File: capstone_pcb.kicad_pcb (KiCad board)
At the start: 4 copper layers, 60.2 x 43.6 mm, 43 parts, among them IC6 BSS138, Q1 BSS138, U2 BMI270, U3 NRF52840-QIAA-R, U4 MAX30102, U5 AMS1117-1.8, U6 TPS61099DRV, X1 32MHz, X2 32.768kHz

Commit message: update pcb layout
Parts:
- moved C23 28.8 mm to (116.2, 64.7), turned to -90 degrees
- moved R7 26.2 mm to (116.2, 67.7), turned to 90 degrees
- moved C24 23.8 mm to (100.3, 50.3), turned to -90 degrees
- moved U4 21.0 mm to (112.2, 65.7), turned to 0 degrees
- moved R8 19.5 mm to (108.3, 50.2), turned to -90 degrees
- moved R9 19.5 mm to (108.3, 48.4)
- moved U5 19.4 mm to (114.8, 53.6), turned to -90 degrees
- moved U6 19.0 mm to (104.3, 50.3)
- moved R6 16.8 mm to (107.4, 64.5), turned to 90 degrees
- moved R4 11.4 mm to (107.4, 67.7), turned to -90 degrees
- moved BT1 9.00 mm to (93.3, 65.7), turned to -90 degrees
- moved X1 3.59 mm to (128.4, 71.1), turned to 90 degrees
- moved C1 2.16 mm to (130.9, 72.1), turned to 180 degrees
- moved C2 0.55 mm to (125.9, 72.1), turned to 0 degrees
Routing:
- net +1V8: track 83.7 -> 51.0 mm, vias 4 -> 3
- net /BSDA: track 9.35 -> 27.4 mm, vias 1 -> 2
- net /BSCL: track 9.48 -> 13.9 mm
- net +3V3: track 59.9 -> 62.5 mm, vias 12 -> 11
- net Net-(U3-XC2): track 7.67 -> 5.27 mm
- net +3V: track 10.9 -> 12.7 mm
- net Net-(U3-XC1): track 8.40 -> 7.28 mm
- net GND: track 61.3 -> 61.2 mm, vias 18 -> 21

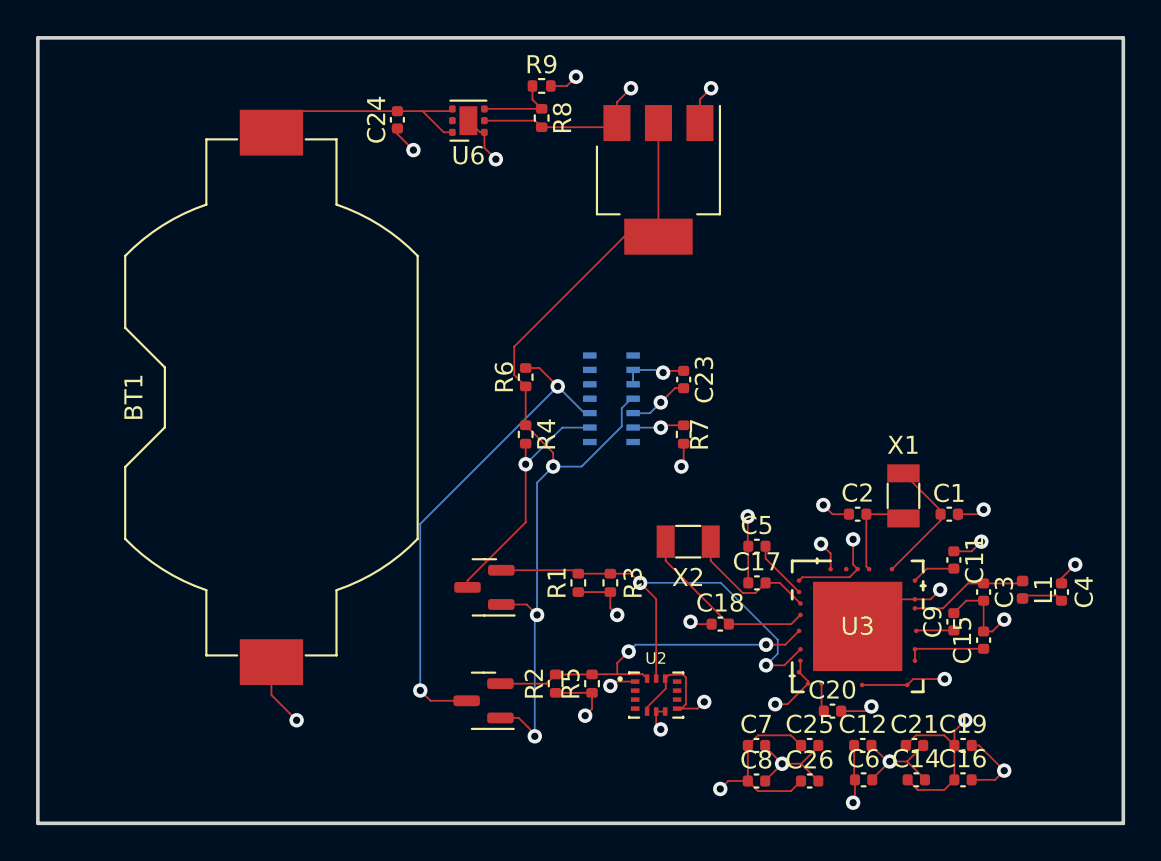
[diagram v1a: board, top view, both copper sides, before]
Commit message: add LCSC part numbers
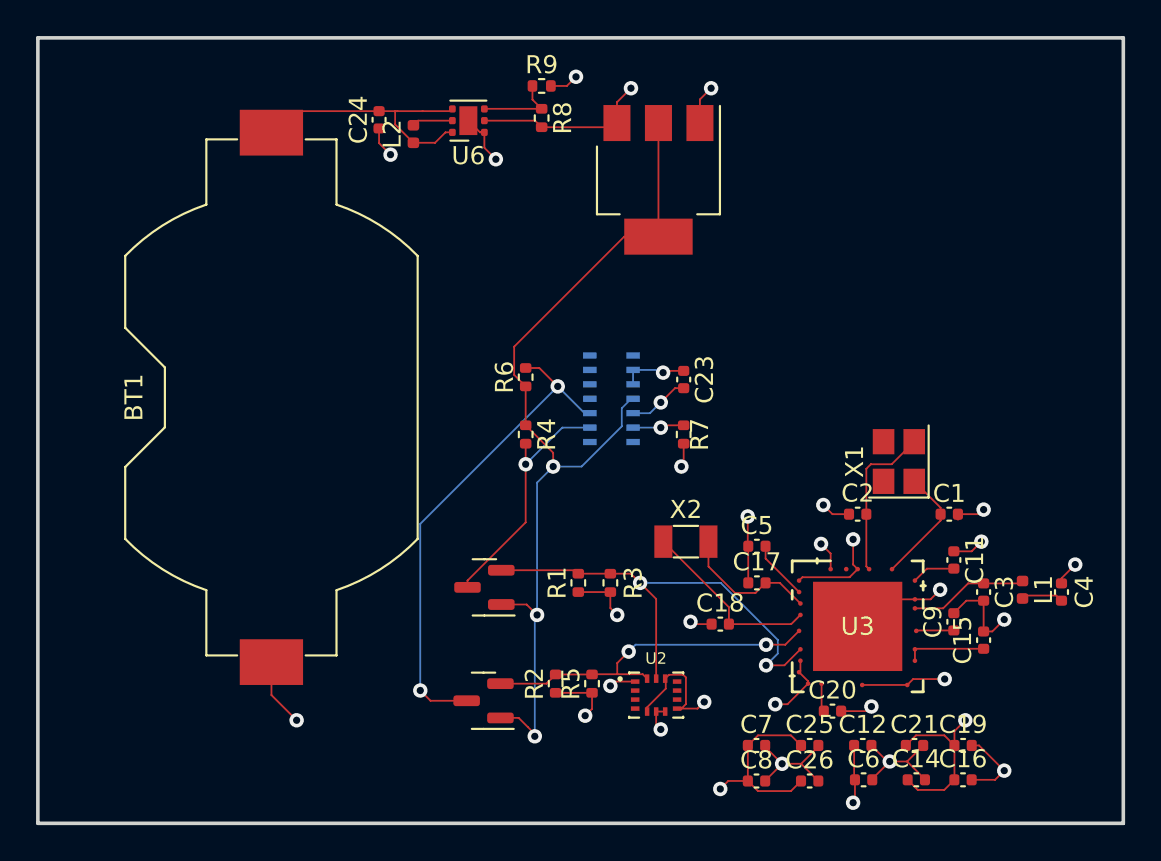
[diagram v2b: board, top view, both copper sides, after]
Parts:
- added L2: 2.2uH, Inductor_SMD:L_0402_1005Metric, F.Cu at (101.2, 51.1)
- C23: value 0.1uF -> 100nF
- R8: value 1.35M -> 453k
- R9: value 300k -> 100k
- U4: value MAX30102 -> MAX30102EFD+T
- X1: footprint Crystal:Crystal_SMD_3215-2Pin_3.2x1.5mm -> Crystal:Crystal_SMD_3225-4Pin_3.2x2.5mm
- moved X1 1.92 mm to (128.1, 69.2)
- moved C24 1.02 mm to (99.3, 50.3)
- moved X2 0.13 mm to (116.3, 73.7)
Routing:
- net Net-(U3-XC2): track 5.27 -> 8.91 mm
- net +3V: track 12.7 -> 15.2 mm
- net Net-(U6-SW): track 0.00 -> 2.27 mm
- net Net-(U3-XC1): track 7.28 -> 6.59 mm
